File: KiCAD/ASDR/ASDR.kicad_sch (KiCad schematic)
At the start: 40 parts, among them J1 OUT, J2 Conn_01x03, J3 Conn_01x03, J4 OUT, J5 OUT, Q1 BC550, Q2 BC550, Q3 BC550, Q4 BC547, SW1 SW_SPDT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

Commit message: ADSR PCB
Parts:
- D1, D2, D3, D4: footprint HackSynth:D_A-405_P7.62mm_Horizontal -> HackSynth:D_DO-35_SOD27_P7.62mm_Horizontal
- J1: value OUT -> IN
- RV1: value 10k -> SUSTAIN 10k
- RV2: value 1M -> DECAY 1M
- RV3: value 1M -> ATTACK 1M
- RV4: value 1M -> RELEASE 1M
- U1: footprint Package_DIP:DIP-8_W7.62mm -> HackSynth:DIP-8_W7.62mm_LongPads
- renumbered J4 to J2, J5 to J3, J2 to J4, J3 to J5
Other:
- note removed: "ATTACK"
- note removed: "DECAY"
- note removed: "RELEASE"
- note removed: "SUSTAIN"
- moved on the sheet: J1, Q1, R1, R2, R3, R4

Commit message: Review
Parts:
- R7, R8: value 100 -> 100R
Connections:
- net GND: now also J1.G, J1.S
- net at D2.1 (K), RV2.2: now also RV2.3; no longer RV2.1
- net at R10.1: now also RV2.1; no longer RV2.3
- net at R8.1, RV4.2: now also RV4.3; no longer RV4.1
- net at R7.1, RV3.2: now also RV3.3; no longer RV3.1
- net at D3.2 (A): now also RV3.1; no longer RV3.3
- net at D4.1 (K): now also RV4.1; no longer RV4.3
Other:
- moved on the sheet: RV2, RV3, RV4
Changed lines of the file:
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@@
 		(color 0 0 0 0)
 	)
+	(junction
+		(at 33.02 105.41)
+		(diameter 0)
+		(color 0 0 0 0)
+	)
 	(wire
 		(pts
@@
 	(wire
 		(pts
+			(xy 33.02 105.41) (xy 33.02 118.11)
+		)
+		(stroke
+			(width 0)
+			(type default)
+		)
+	)
+	(wire
+		(pts
 			(xy 266.7 100.33) (xy 274.32 100.33)
 		)
@@
 	)
 	(image
-		(at -68.58 95.25)
+		(at 182.245 10.795)
 		(scale 0.396342)
 		(data "iVBORw0KGgoAAAANSUhEUgAACOoAAASyCAYAAAACxZaCAAAAAXNSR0IArs4c6QAAAARnQU1BAACx"
@@
 	(symbol
 		(lib_id "HackSynth:R_Potentiometer")
-		(at 173.99 77.47 90)
-		(mirror x)
+		(at 173.99 77.47 270)
 		(unit 1)
 		(exclude_from_sim no)
@@
 		(on_board yes)
 		(dnp no)
-		(fields_autoplaced yes)
 		(property "Reference" "RV2"
 			(at 173.99 71.12 90)
@@
 			)
 		)
-		(property "Value" "100"
+		(property "Value" "100R"
 			(at 163.83 108.204 90)
 			(effects
@@
 	(symbol
 		(lib_id "HackSynth:R_Potentiometer")
-		(at 173.99 95.25 90)
-		(mirror x)
+		(at 173.99 95.25 270)
 		(unit 1)
 		(exclude_from_sim no)
@@
 		(on_board yes)
 		(dnp no)
-		(fields_autoplaced yes)
 		(property "Reference" "RV3"
 			(at 173.99 88.9 90)
@@
 	)
 	(symbol
+		(lib_id "power:GND")
+		(at 33.02 118.11 0)
+		(unit 1)
+		(exclude_from_sim no)
+		(in_bom yes)
+		(on_board yes)
+		(dnp no)
+		(property "Reference" "#PWR028"
+			(at 33.02 124.46 0)
+			(effects
+				(font
+					(size 1.27 1.27)
+				)
+				(hide yes)
+			)
+		)
+		(property "Value" "GND"
+			(at 33.02 123.19 0)
+			(effects
+				(font
+					(size 1.27 1.27)
+				)
+			)
+		)
+		(property "Footprint" ""
+			(at 33.02 118.11 0)
+			(effects
+				(font
+					(size 1.27 1.27)
+				)
+				(hide yes)
+			)
+		)
+		(property "Datasheet" ""
+			(at 33.02 118.11 0)
+			(effects
+				(font
+					(size 1.27 1.27)
+				)
+				(hide yes)
+			)
+		)
+		(property "Description" "Power symbol creates a global label with name \"GND\" , ground"
+			(at 33.02 118.11 0)
+			(effects
+				(font
+					(size 1.27 1.27)
+				)
+				(hide yes)
+			)
+		)
+		(pin "1"
+		)
+		(instances
+			(project "ASDR"
+				(path "/6d643dfc-e3ba-4819-8915-ad269ac53831"
+					(reference "#PWR028")
+					(unit 1)
+				)
+			)
+		)
+	)
+	(symbol
 		(lib_id "Transistor_BJT:BC550")
 		(at 55.88 100.33 0)
@@
 	(symbol
 		(lib_id "HackSynth:R_Potentiometer")
-		(at 173.99 113.03 90)
-		(mirror x)
+		(at 173.99 113.03 270)
 		(unit 1)
 		(exclude_from_sim no)
@@
 		(on_board yes)
 		(dnp no)
-		(fields_autoplaced yes)
 		(property "Reference" "RV4"
 			(at 173.99 106.68 90)
@@
 			)
 		)
-		(property "Value" "100"
+		(property "Value" "100R"
 			(at 163.576 90.424 90)
 			(effects

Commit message: VCF PCB
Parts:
- added J6: Conn_02x05_Odd_Even, symbol Connector_Generic:Conn_02x05_Odd_Even
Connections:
- net GND: now also J6.3 (Pin_3), J6.4 (Pin_4), J6.5 (Pin_5), J6.6 (Pin_6), J6.7 (Pin_7), J6.8 (Pin_8)
- net VDD: now also J6.1 (Pin_1), J6.2 (Pin_2)
- net VSS: now also J6.10 (Pin_10), J6.9 (Pin_9)

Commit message: VCF PCB
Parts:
- C2: footprint HackSynth:CP_Radial_D5.2mm_P2.50mm_LayDown -> HackSynth:CP_Radial_D4.0mm_P1.50mm
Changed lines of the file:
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@@
 			)
 		)
-		(property "Footprint" "HackSynth:CP_Radial_D5.2mm_P2.50mm_LayDown"
+		(property "Footprint" "HackSynth:CP_Radial_D4.0mm_P1.50mm"
 			(at 120.65 100.33 0)
 			(effects

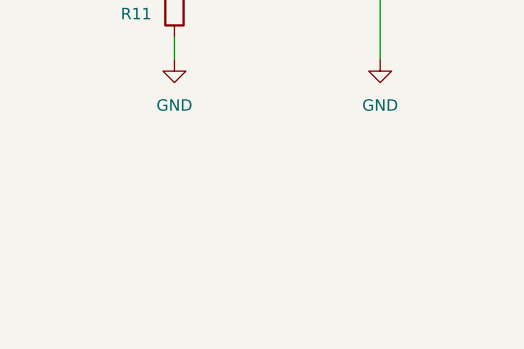
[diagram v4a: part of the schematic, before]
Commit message: Footprint Edits
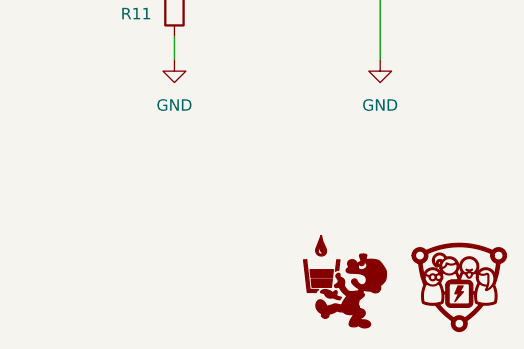
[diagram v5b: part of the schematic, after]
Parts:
- added G1: ~, symbol HackSynth:CCHS_Logo
- added G2: ~, symbol HackSynth:Logo_PancakeLegend
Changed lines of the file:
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@@
 	)
 	(symbol
+		(lib_id "HackSynth:CCHS_Logo")
+		(at 275.59 172.72 0)
+		(unit 1)
+		(exclude_from_sim no)
+		(in_bom yes)
+		(on_board yes)
+		(dnp no)
+		(fields_autoplaced yes)
+		(property "Reference" "G1"
+			(at 275.59 180.34 0)
+			(effects
+				(font
+					(size 1.27 1.27)
+				)
+				(hide yes)
+			)
+		)
+		(property "Value" "~"
+			(at 281.94 173.89 0)
+			(effects
+				(font
+					(size 1.27 1.27)
+				)
+				(justify left)
+			)
+		)
+		(property "Footprint" ""
+			(at 275.59 172.72 0)
+			(effects
+				(font
+					(size 1.27 1.27)
+				)
+				(hide yes)
+			)
+		)
+		(property "Datasheet" ""
+			(at 275.59 172.72 0)
+			(effects
+				(font
+					(size 1.27 1.27)
+				)
+				(hide yes)
+			)
+		)
+		(property "Description" ""
+			(at 275.59 172.72 0)
+			(effects
+				(font
+					(size 1.27 1.27)
+				)
+				(hide yes)
+			)
+		)
+		(instances
+			(project "ASDR"
+				(path "/6d643dfc-e3ba-4819-8915-ad269ac53831"
+					(reference "G1")
+					(unit 1)
+				)
+			)
+		)
+	)
+	(symbol
 		(lib_id "HackSynth:R")
 		(at 82.55 81.28 180)
@@
 				)
 			)
+		)
+	)
+	(symbol
+		(lib_id "HackSynth:Logo_PancakeLegend")
+		(at 262.89 173.355 0)
+		(unit 1)
+		(exclude_from_sim no)
+		(in_bom yes)
+		(on_board yes)
+		(dnp no)
+		(fields_autoplaced yes)
+		(property "Reference" "G2"
+			(at 262.89 180.975 0)
+			(effects
+				(font
+					(size 1.27 1.27)
+				)
+				(hide yes)
+			)
+		)
+		(property "Value" "~"
+			(at 269.24 173.2549 0)
+			(effects
+				(font
+					(size 1.27 1.27)
+				)
+				(justify left)
+			)
+		)
+		(property "Footprint" ""
+			(at 262.89 173.355 0)
+			(effects
+				(font
+					(size 1.27 1.27)
+				)
+				(hide yes)
+			)
+		)
+		(property "Datasheet" ""
+			(at 262.89 173.355 0)
+			(effects
+				(font
+					(size 1.27 1.27)
+				)
+				(hide yes)
+			)
+		)
+		(property "Description" ""
+			(at 262.89 173.355 0)
+			(effects
+				(font
+					(size 1.27 1.27)
+				)
+				(hide yes)
+			)
+		)
+		(instances
+			(project "ASDR"
+				(path "/6d643dfc-e3ba-4819-8915-ad269ac53831"
+					(reference "G2")
+					(unit 1)
+				)
+			)
